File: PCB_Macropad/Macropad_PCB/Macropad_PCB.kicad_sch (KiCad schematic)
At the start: 0 parts

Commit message: update latest
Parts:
- added SW1, SW2: RotaryEncoder_Switch, symbol Device:RotaryEncoder_Switch
- added U1: ESP32-C3_SUPERMINI_TH, ESP32-C3_SUPERMINI_TH:MODULE_ESP32-C3_SUPERMINI_TH, symbol ESP32-C3_SUPERMINI_TH:ESP32-C3_SUPERMINI_TH
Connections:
- new net D0: U1.0 (GPIO0)
- new net D1: U1.1 (GPIO1)
- new net D10: SW2.B, U1.10 (GPIO10)
- new net D2: U1.2 (GPIO2)
- new net D20: U1.20 (GPIO20)
- new net D21: U1.21 (GPIO21)
- new net D3: U1.3 (GPIO3)
- new net D4: U1.4 (GPIO4)
- new net D5: SW1.S1, U1.5 (GPIO5)
- new net D6: SW1.A, U1.6 (GPIO6)
- new net D7: SW1.B, U1.7 (GPIO7)
- new net D8: SW2.S1, U1.8 (GPIO8)
- new net D9: SW2.A, U1.9 (GPIO9)
- new net GND: SW1.C, SW1.S2, SW2.C, SW2.S2, U1.G (GND)

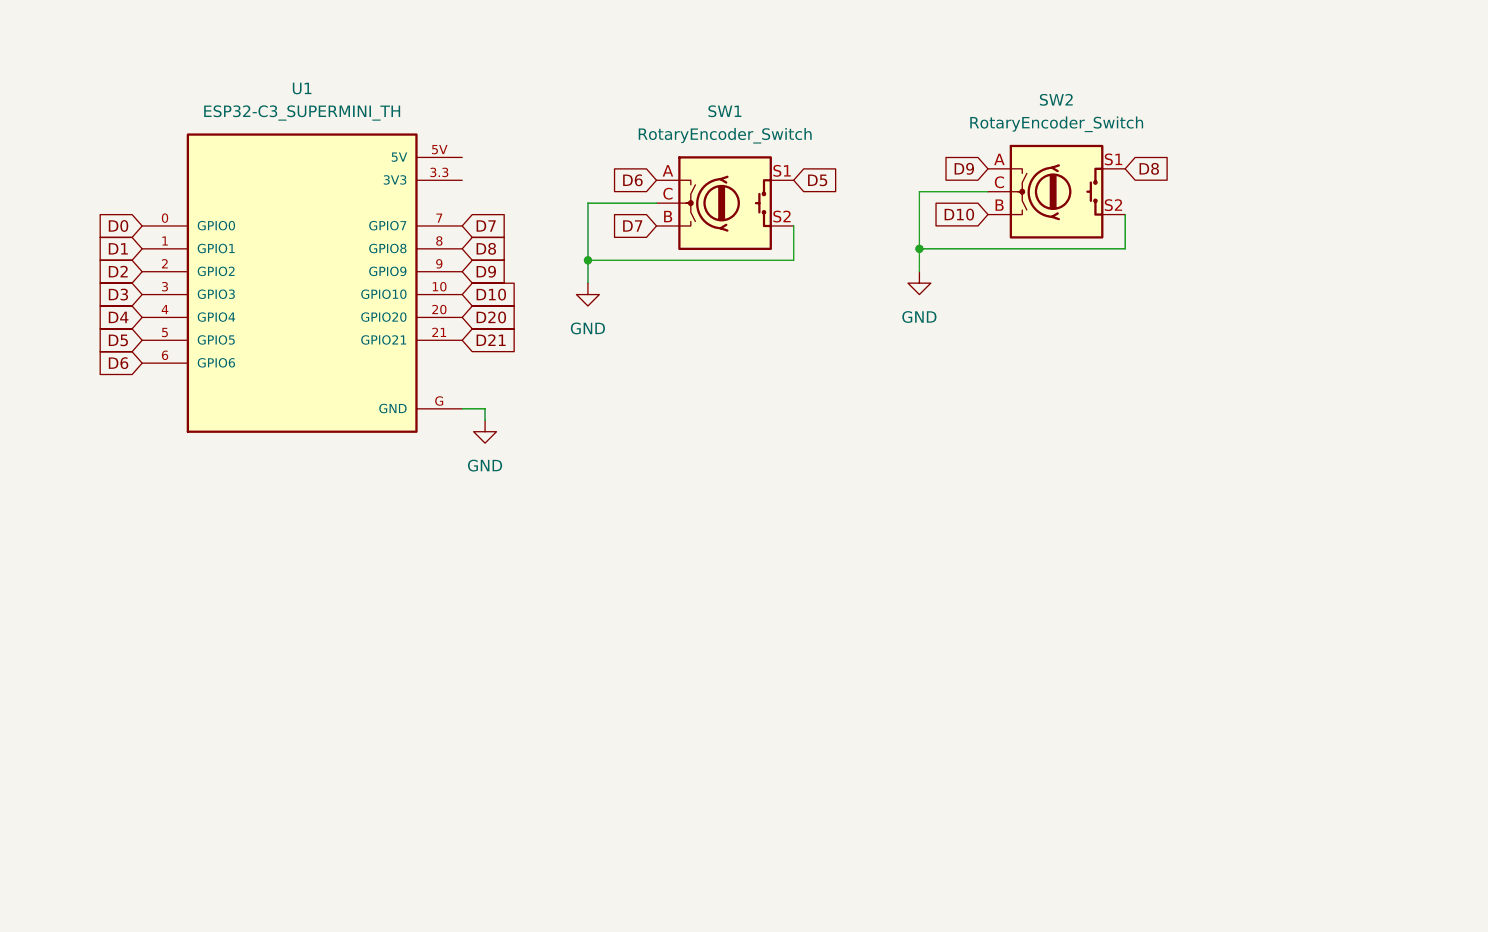
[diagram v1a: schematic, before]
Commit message: Add netlist file for PCB Macropad with detailed component connections
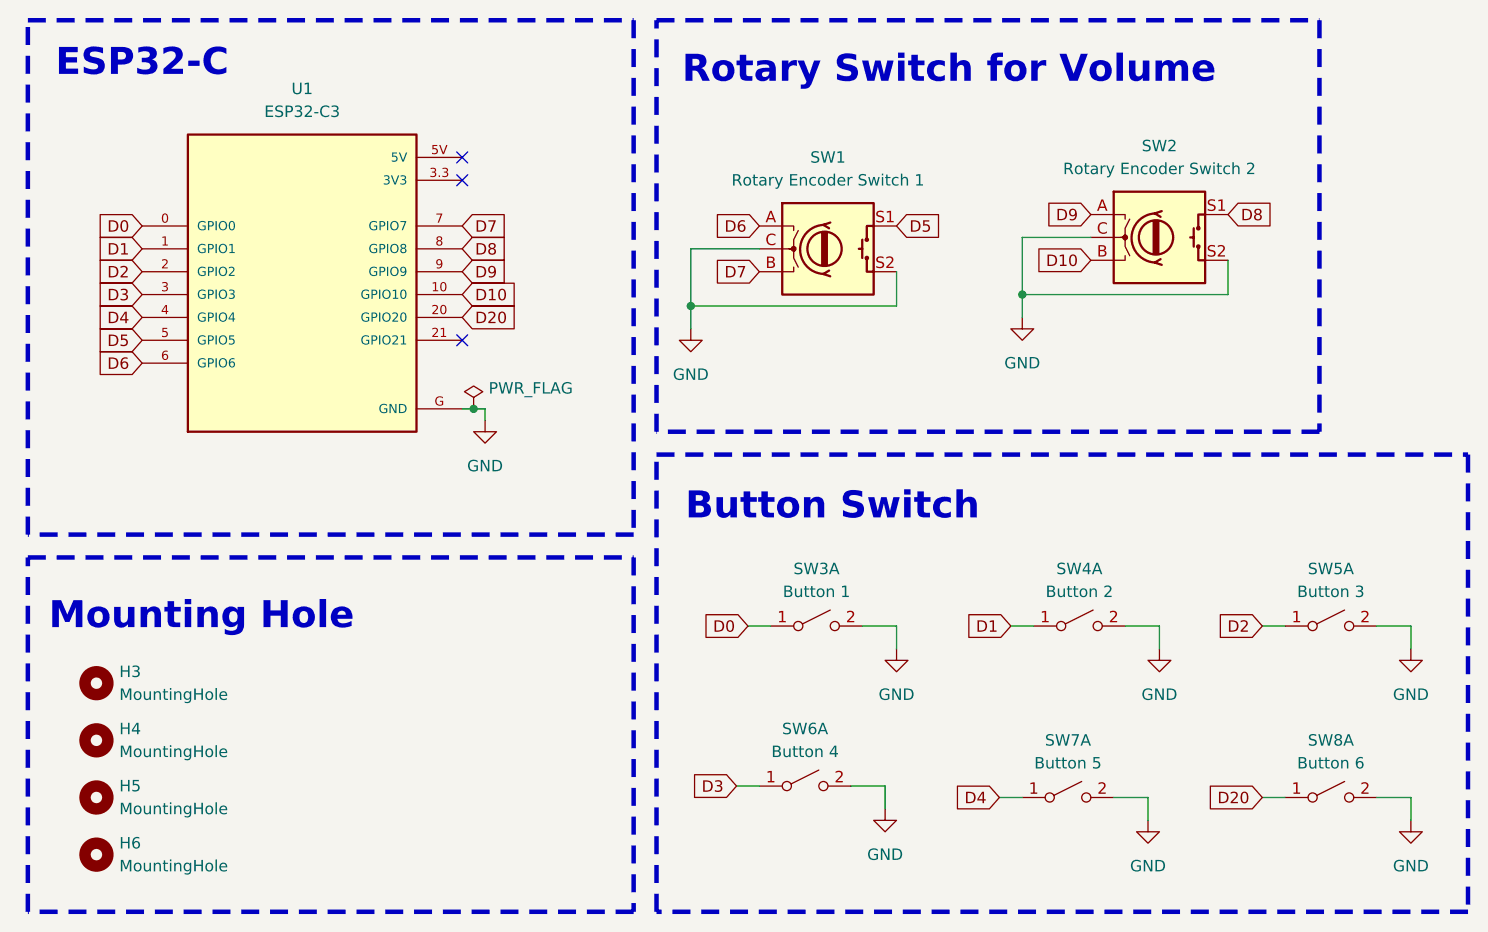
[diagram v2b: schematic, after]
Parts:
- added H3, H4, H5, H6: MountingHole, MountingHole:MountingHole_3mm_Pad_Via, symbol Mechanical:MountingHole
- added SW3: Button 1, AC MechanicalSwtich:SW_Cherry_MX_PCB_1.00u, symbol Switch:SW_DPST_x2
- added SW4: Button 2, AC MechanicalSwtich:SW_Cherry_MX_PCB_1.00u, symbol Switch:SW_DPST_x2
- added SW5: Button 3, AC MechanicalSwtich:SW_Cherry_MX_PCB_1.00u, symbol Switch:SW_DPST_x2
- added SW6: Button 4, AC MechanicalSwtich:SW_Cherry_MX_PCB_1.00u, symbol Switch:SW_DPST_x2
- added SW7: Button 5, AC MechanicalSwtich:SW_Cherry_MX_PCB_1.00u, symbol Switch:SW_DPST_x2
- added SW8: Button 6, AC MechanicalSwtich:SW_Cherry_MX_PCB_1.00u, symbol Switch:SW_DPST_x2
- SW1: value RotaryEncoder_Switch -> Rotary Encoder Switch 1; footprint (none) -> Rotary_Encoder:RotaryEncoder_Alps_EC11E-Switch_Vertical_H20mm
- SW2: value RotaryEncoder_Switch -> Rotary Encoder Switch 2; footprint (none) -> Rotary_Encoder:RotaryEncoder_Alps_EC11E-Switch_Vertical_H20mm
- U1: value ESP32-C3_SUPERMINI_TH -> ESP32-C3
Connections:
- net D0: now also SW3.1 (A)
- net D1: now also SW4.1 (A)
- net D2: now also SW5.1 (A)
- net D20: now also SW8.1 (A)
- net D3: now also SW6.1 (A)
- net D4: now also SW7.1 (A)
- net GND: now also SW3.2 (B), SW4.2 (B), SW5.2 (B), SW6.2 (B), SW7.2 (B), SW8.2 (B)
- net D21: no longer names the net of U1.21 (GPIO21)
- no-connect marks 0 -> 3
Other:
- note added: "Button Switch"
- note added: "ESP32-C"
- note added: "Mounting Hole"
- note added: "Rotary Switch for Volume"
- moved on the sheet: SW1, SW2
